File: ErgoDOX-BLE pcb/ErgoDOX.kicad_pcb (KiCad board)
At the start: 2 copper layers, 182.8 x 158.9 mm, 110 parts, among them J1 Conn_01x04, J2 Conn_01x02_Female, J3 Conn_01x02_Female, J4 Conn_01x02, J5 Conn_01x02, P1 USB_C_Plug_USB2.0, Q1 Q_NPN_BCE, SW0:10 SW0:3, SW0:11 SW0:2, SW0:12 SW0:1, SW0:7 SW0:6, SW0:8 SW0:5, SW0:9 SW0:4, SW1:10 SW1:3, SW1:11 SW1:2, SW1:12 SW1:1, SW1:13 SW1:0, SW1:9 SW1:4, SW2:10 SW2:3, SW2:11 SW2:2, SW2:12 SW2:1, SW2:13 SW2:0, SW2:7 SW2:6, SW2:8 SW2:5, SW2:9 SW2:4, SW3:10 SW3:3, SW3:11 SW3:2, SW3:12 SW3:1, SW3:13 SW3:0, SW3:8 SW3:5, SW3:9 SW3:4, SW4:10 SW4:3, SW4:11 SW4:2, SW4:12 SW4:1, SW4:13 SW4:0, SW4:7 SW4:6, SW4:8 SW4:5, SW4:9 SW4:4, SW5:10 SW5:3, SW5:11 SW5:2, SW5:12 SW5:1, SW5:13 SW5:0, SW5:7 SW5:6, SW5:8 SW5:5, SW5:9 SW5:4, U1 MCP23018, U3 C0720B001F

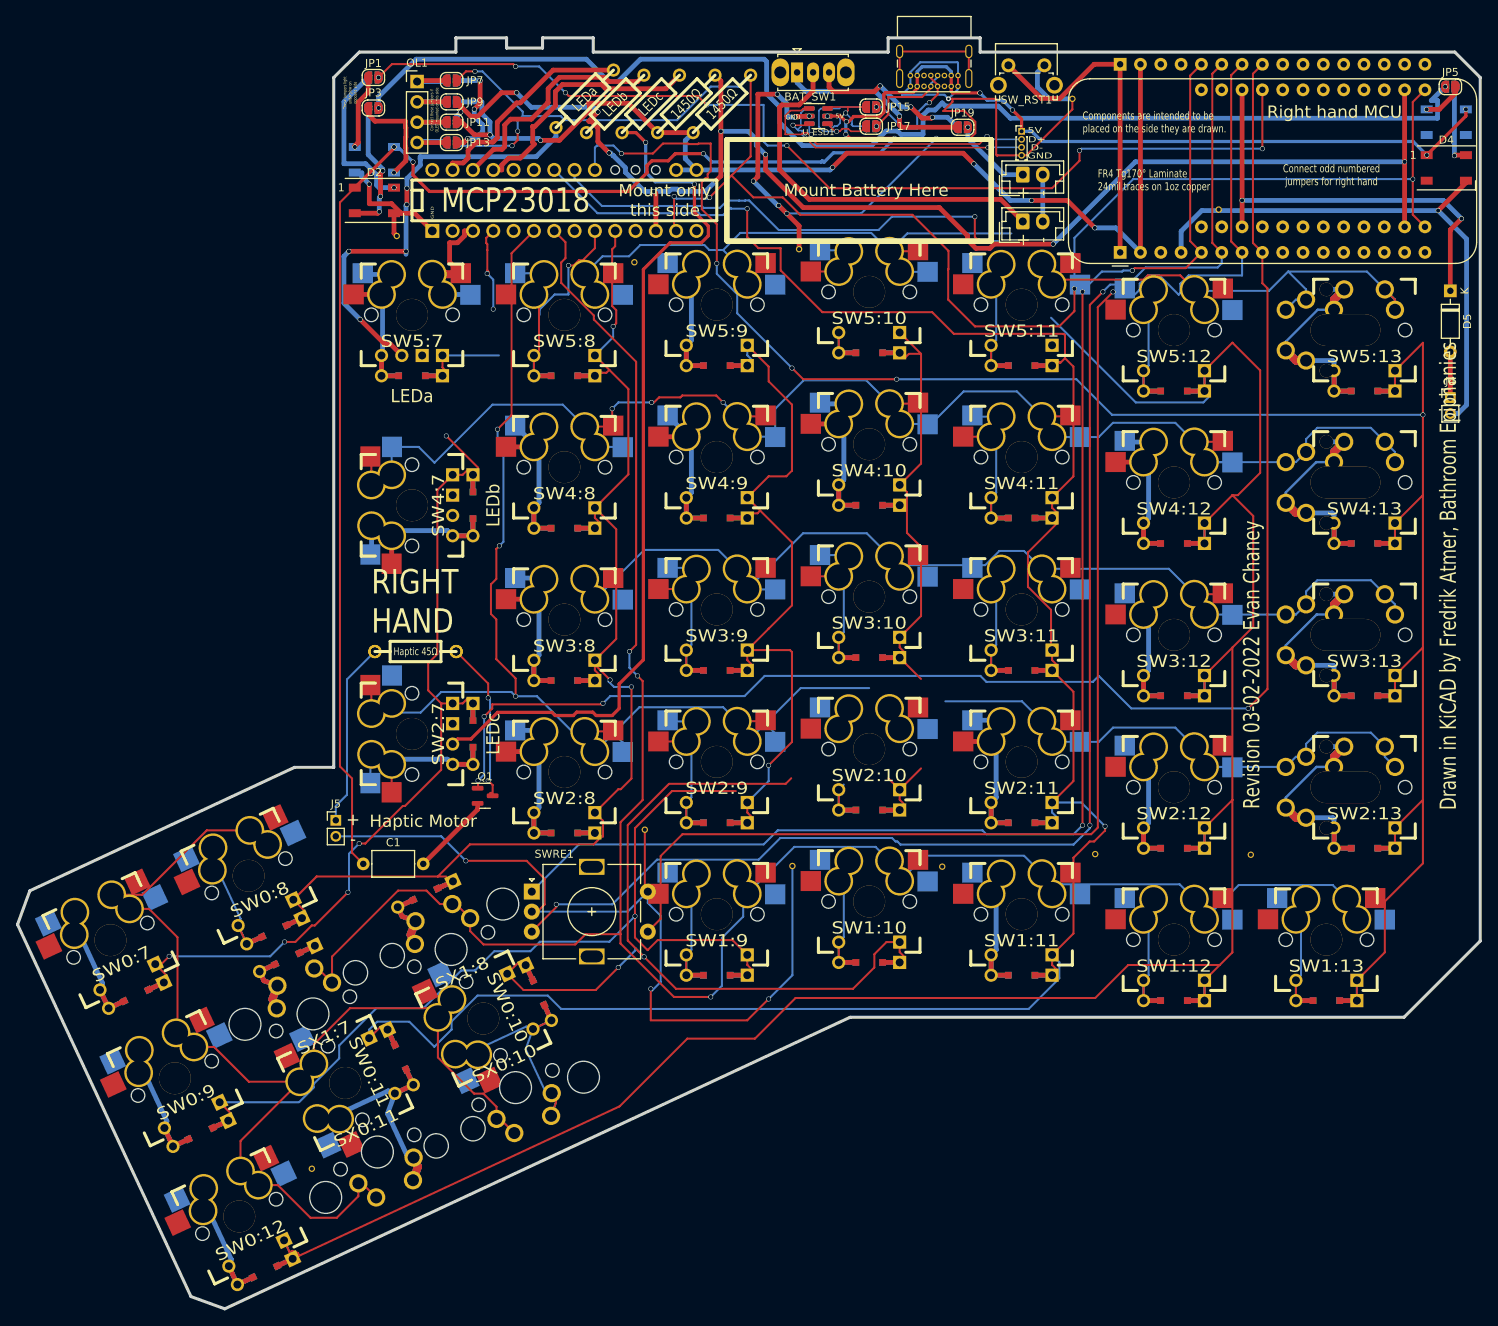
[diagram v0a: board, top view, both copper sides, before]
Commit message: Make the pads for kailh hot swaps the correct side
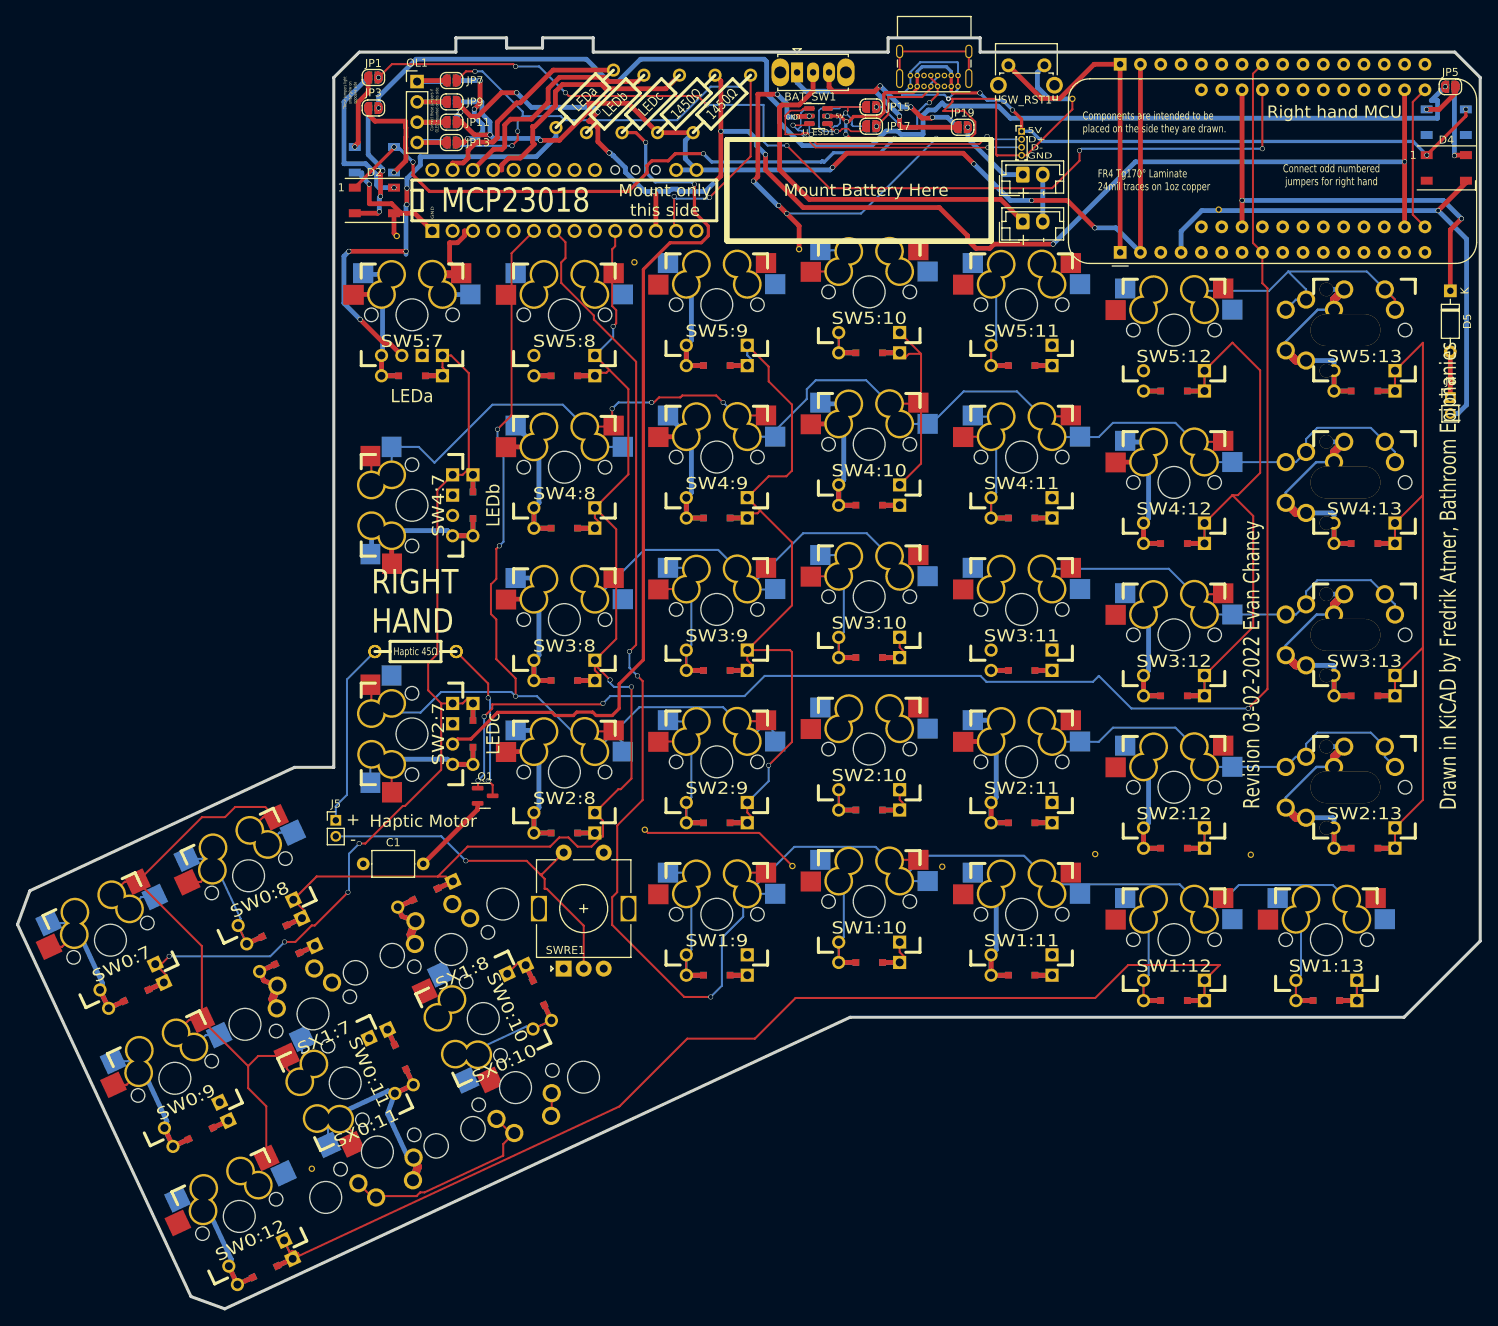
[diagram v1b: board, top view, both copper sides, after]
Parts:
- moved SWRE1 10.4 mm to (91.4, 146.8), turned to 90 degrees
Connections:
- C1 pad 1: +5V -> +3V3
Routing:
- net /ROW4: track 2683.5 -> 177.3 mm, vias 27 -> 3
- net /SDA: track 388.5 -> 98.1 mm, vias 10 -> 5
- net /ROW1: track 0.00 -> 229.0 mm, vias 0 -> 3
- net /COL5: track 0.00 -> 189.5 mm, vias 0 -> 3
- net /COL1: track 60.9 -> 218.7 mm, vias 2 -> 0
- net /ROW3: track 0.00 -> 107.7 mm
- net /ROW0: track 0.00 -> 103.9 mm
- net /COL0: track 0.00 -> 102.3 mm
- net +5V: track 266.9 -> 179.9 mm
- net /COL3: track 110.0 -> 32.0 mm, vias 2 -> 0
- net /ROW5: track 18.8 -> 66.1 mm
- net GND: track 221.2 -> 266.9 mm, vias 13 -> 14
- net Net-(SW2:9-Pad2): track 0.00 -> 22.9 mm
- net Net-(SW1:9-Pad2): track 0.00 -> 19.5 mm
- net Net-(SW1:13-Pad2): track 0.00 -> 15.9 mm
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
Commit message: Restart my routing mess
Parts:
- moved STITCHING_VIA 0.52 mm to (139.2, 134.1)
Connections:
- STITCHING_VIA pad GND: /COL5 -> (no net)
- STITCHING_VIA pad GND: /COL5 -> GND
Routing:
- net GND: track 266.9 -> 394.3 mm
- net /ROW5: track 66.1 -> 158.1 mm
- net /COL5: track 189.5 -> 169.1 mm
- net Net-(SW5:12-Pad2): track 0.00 -> 16.5 mm
- net Net-(SW0:10-Pad2): track 15.9 -> 31.8 mm
- net /ROW1: track 229.0 -> 236.1 mm
- net Net-(SW1:11-Pad2): track 15.9 -> 23.0 mm
- net Net-(SW1:10-Pad2): track 15.9 -> 23.0 mm
- net /COL2: track 0.00 -> 1.80 mm

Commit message: More routing
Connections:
- SX0:10 pad : /COL5 -> (no net)
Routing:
- net /EncoderPin1: track 0.00 -> 193.1 mm, vias 0 -> 2
- net /EncoderPin2: track 0.00 -> 181.2 mm, vias 0 -> 2
- net /EncoderClick: track 0.00 -> 173.4 mm
- net /COL4: track 83.1 -> 217.4 mm, vias 1 -> 2
- net GND: track 394.3 -> 482.5 mm, vias 14 -> 13
- net /ROW3: track 107.7 -> 173.6 mm
- net /COL5: track 169.1 -> 216.8 mm
- net /ROW0: track 103.9 -> 139.8 mm
- net /ROW2: track 184.7 -> 218.5 mm
- net /COL2: track 1.80 -> 24.3 mm
- net /ROW1: track 236.1 -> 219.3 mm
- net /COL1: track 218.7 -> 230.9 mm
- net Net-(SW5:10-Pad2): track 12.7 -> 21.0 mm
- net Net-(SW0:12-Pad2): track 15.9 -> 23.5 mm
- net Net-(SW2:12-Pad2): track 15.9 -> 23.0 mm
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
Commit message: More routing forever
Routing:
- net GND: track 482.5 -> 660.8 mm, vias 13 -> 14
- net /COL2: track 24.3 -> 179.1 mm
- net /COL0: track 102.3 -> 244.7 mm
- net /COL3: track 32.0 -> 142.0 mm, vias 0 -> 1
- net /ROW5: track 158.1 -> 191.5 mm, vias 0 -> 2
- net /ROW3: track 173.6 -> 197.2 mm
- net /COL4: track 217.4 -> 240.6 mm
- net /ROW2: track 218.5 -> 240.9 mm
- net /ROW4: track 177.3 -> 199.1 mm
- net /COL1: track 230.9 -> 250.7 mm
- net Net-(SW5:8-Pad2): track 0.00 -> 16.5 mm
- net Net-(SW3:11-Pad2): track 7.12 -> 14.7 mm
- net Net-(SW2:10-Pad2): track 15.8 -> 23.4 mm
- net Net-(SW1:12-Pad2): track 15.9 -> 23.0 mm
- net Net-(SW3:12-Pad2): track 15.9 -> 23.0 mm
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
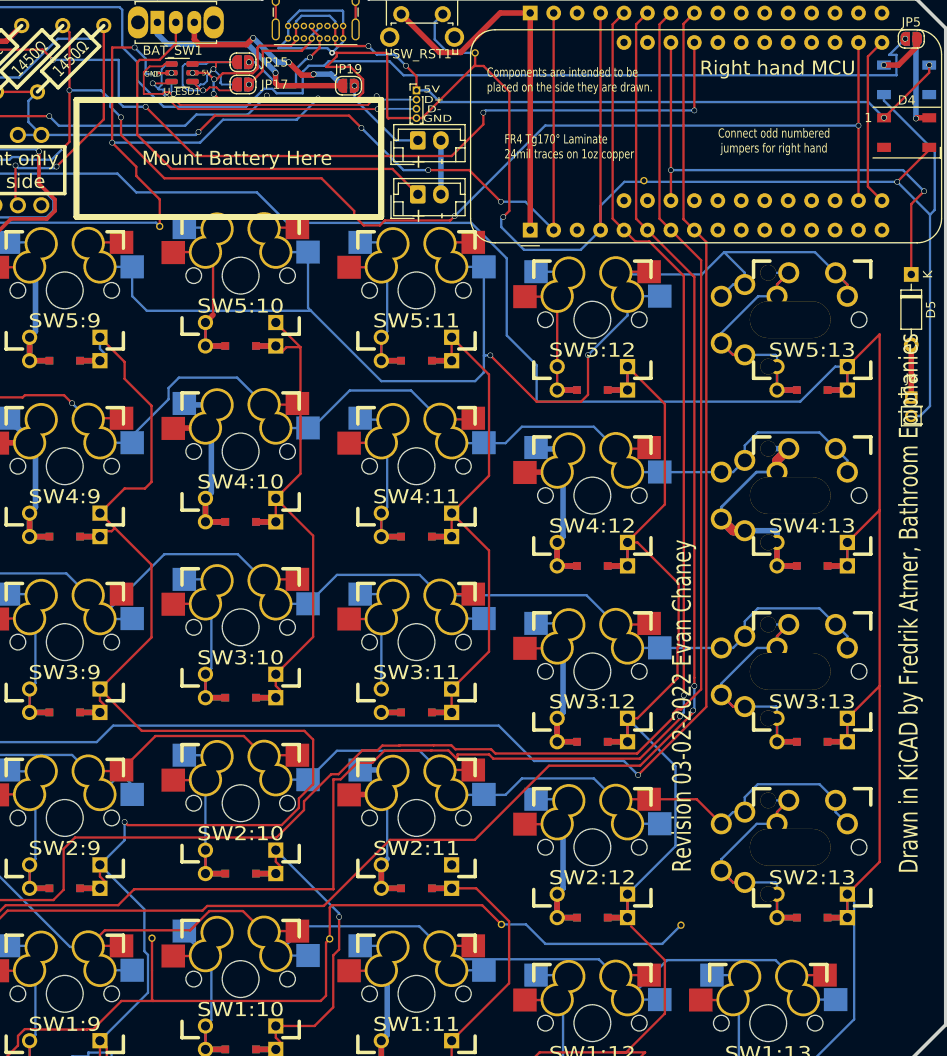
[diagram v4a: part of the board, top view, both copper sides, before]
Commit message: Change edge switches to use the same footprint as the main ones and redo routes
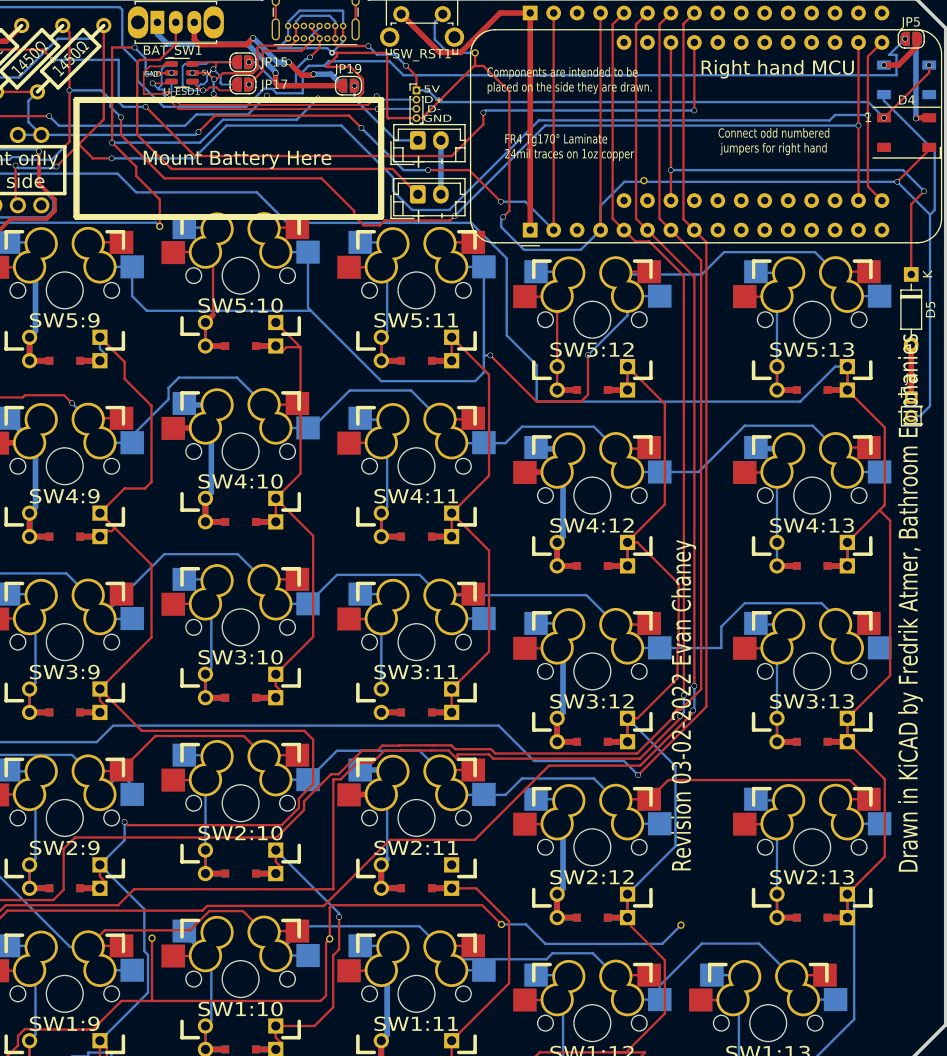
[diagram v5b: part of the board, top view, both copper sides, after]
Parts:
- SW2:13, SW3:13, SW4:13, SW5:13: footprint ErgoDOX pcb:MX_FLIP_XX -> ErgoDOX pcb:MX_FLIP_DIODE_HOTSWAP
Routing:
- net /SDA: track 98.1 -> 194.5 mm, vias 5 -> 7
- net /ROW4: track 199.1 -> 255.8 mm
- net /COL3: track 142.0 -> 92.1 mm
- net /ROW2: track 240.9 -> 271.7 mm
- net Net-(SW2:9-Pad2): track 22.9 -> 0.00 mm
- net /COL0: track 244.7 -> 231.0 mm
- net Net-(SW4:13-Pad2): track 35.2 -> 23.6 mm
- net Net-(SW3:13-Pad2): track 35.2 -> 24.6 mm
- net Net-(SW2:13-Pad2): track 35.2 -> 24.6 mm
- net Net-(SW5:13-Pad2): track 35.1 -> 24.6 mm
- net /ROW3: track 197.2 -> 198.3 mm
- net /ROW1: track 218.7 -> 218.1 mm
